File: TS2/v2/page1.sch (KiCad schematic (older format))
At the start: 25 parts, among them J1 74LS00, SW1 RESET

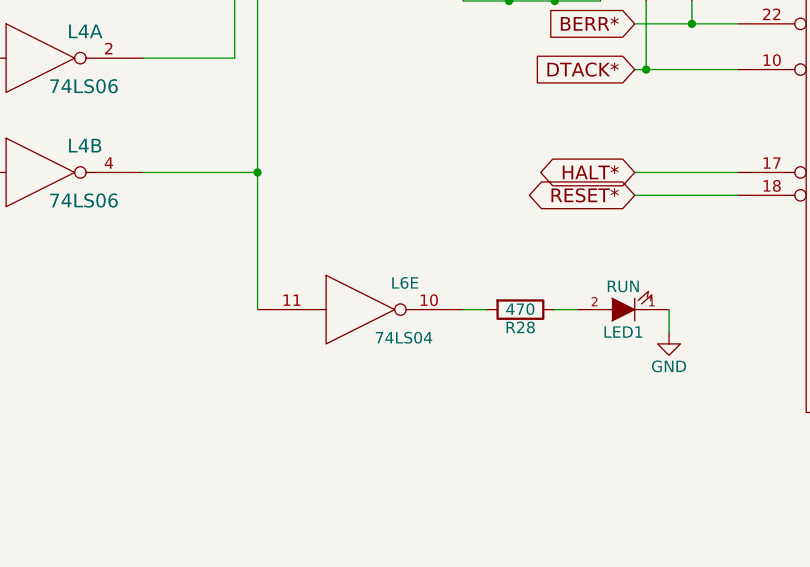
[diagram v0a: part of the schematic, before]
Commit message: Remove extra pages and renumber.
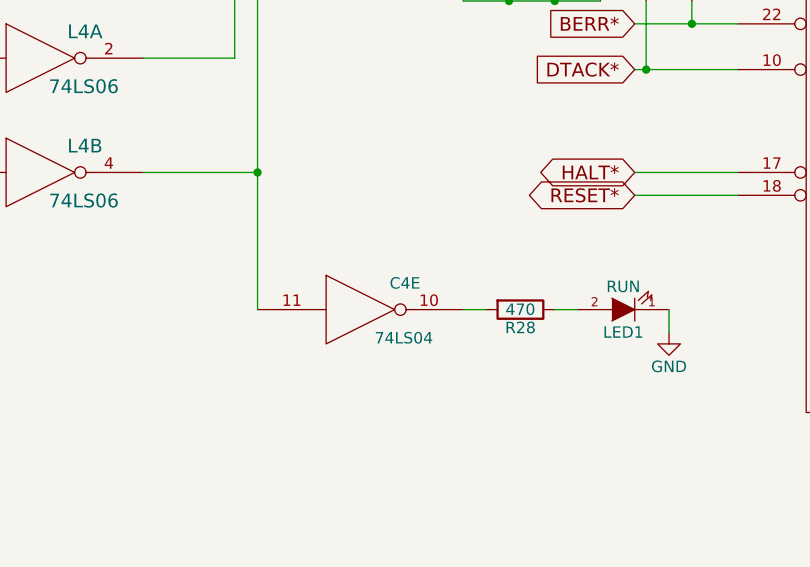
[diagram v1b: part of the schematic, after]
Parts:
- renumbered L6 to C4
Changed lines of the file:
@@
 NoConn ~ 7900 2900
 $Comp
-L 74LS04 L6
+L 74LS04 C4
 U 5 1 57CAED80
 P 6250 5500
-F 0 "L6" H 6445 5615 50  0000 C CNN
+F 0 "C4" H 6445 5615 50  0000 C CNN
 F 1 "74LS04" H 6440 5375 50  0000 C CNN
 F 2 "" H 6250 5500 50  0000 C CNN

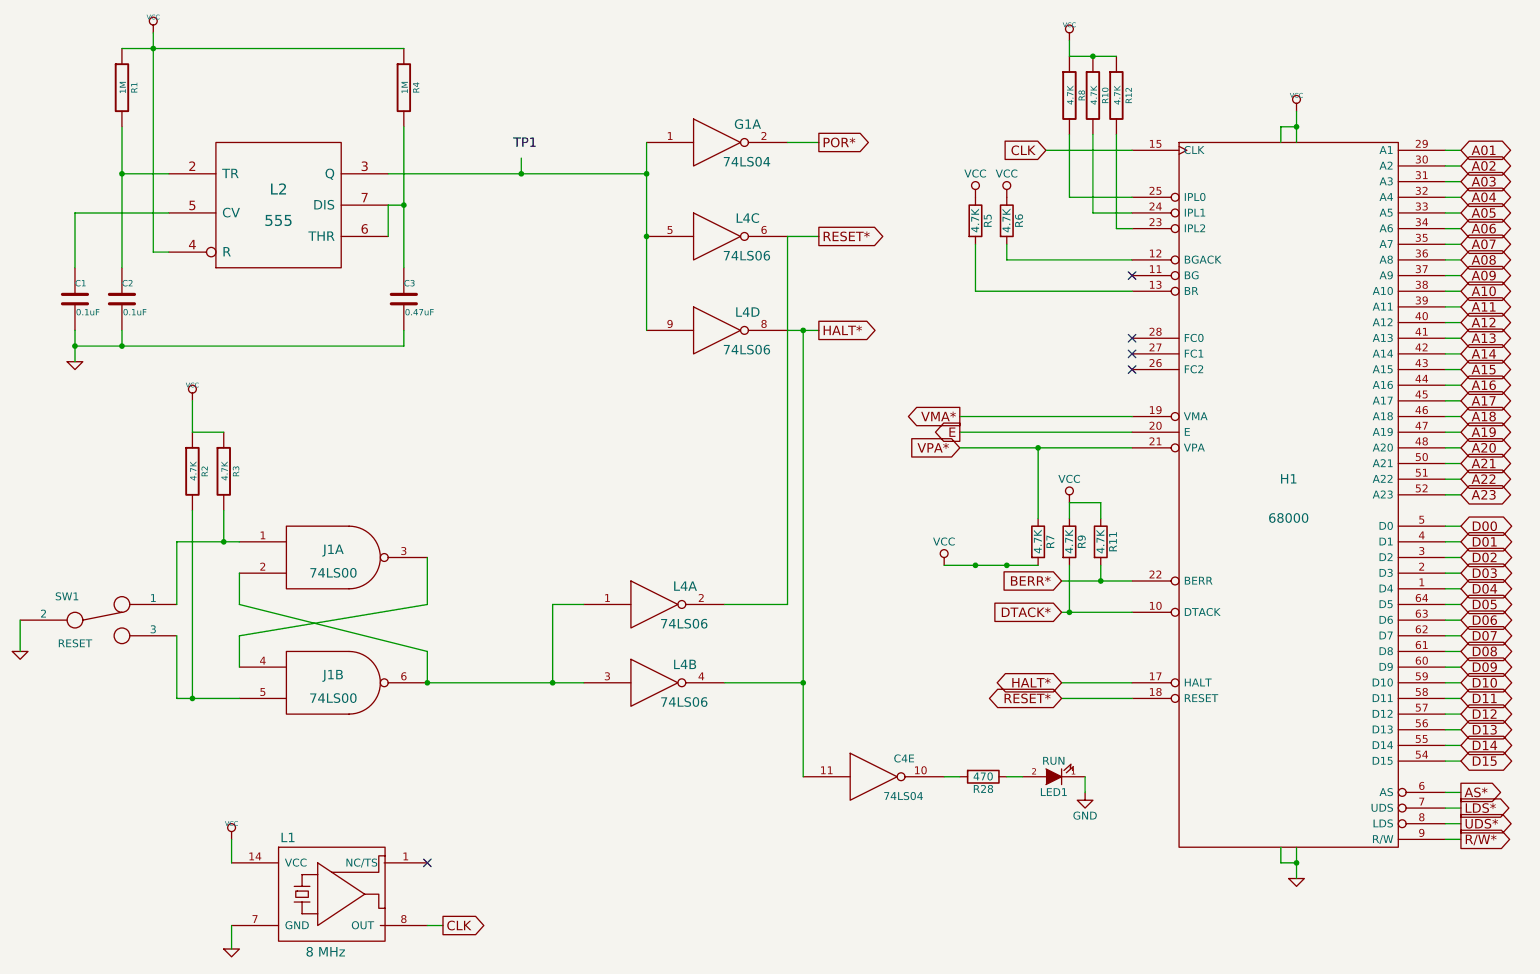
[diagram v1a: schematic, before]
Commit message: more fixup of deleted pages.
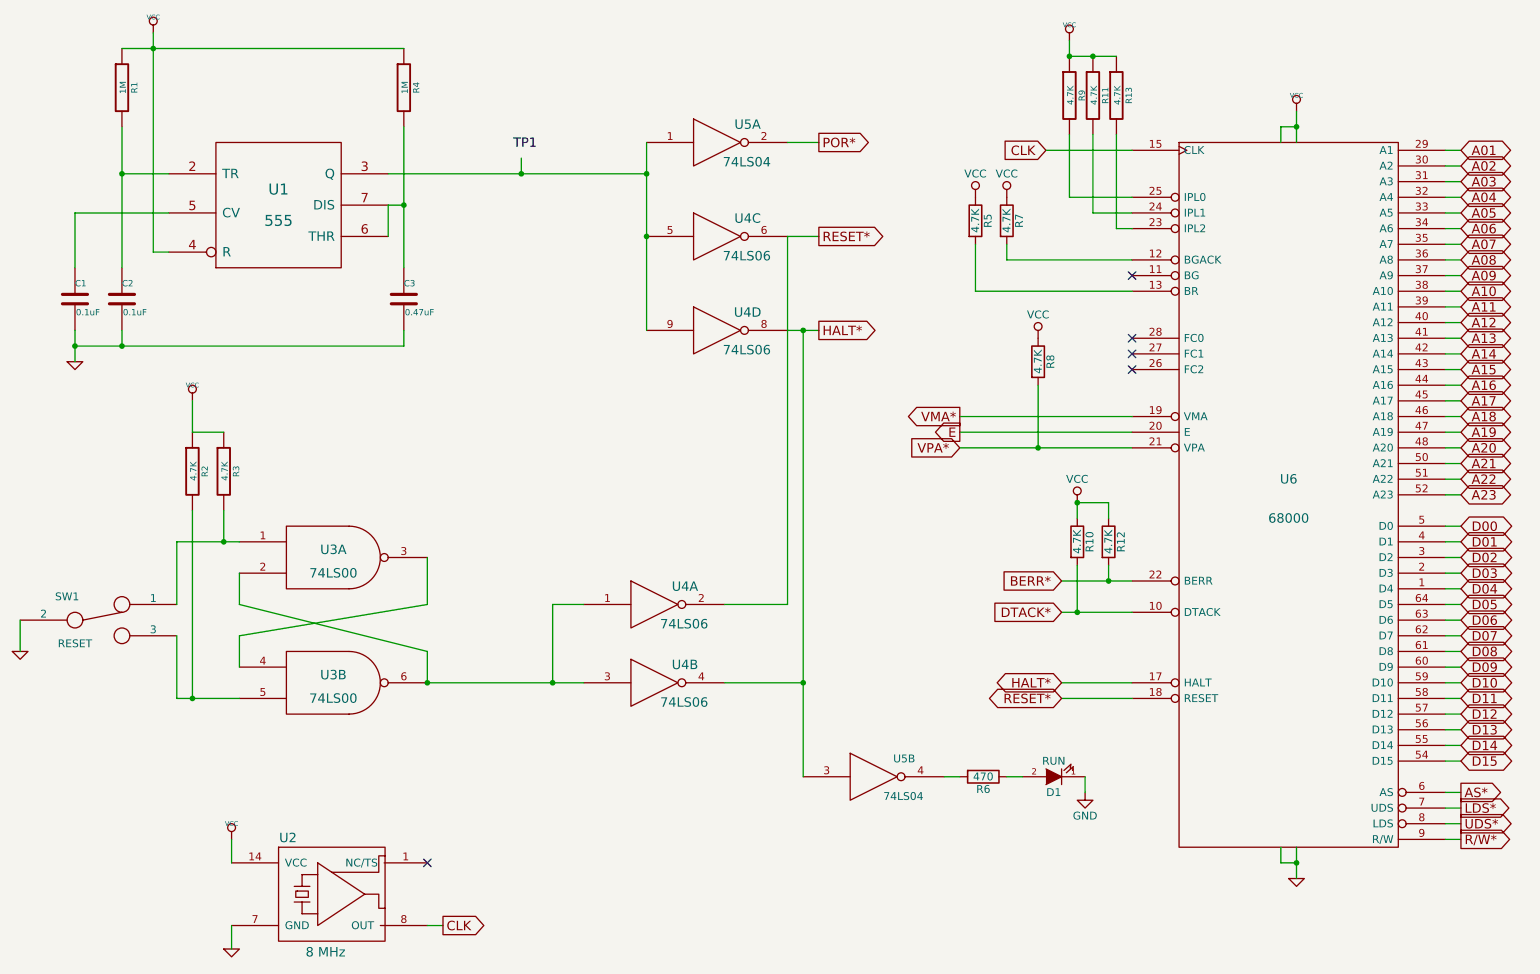
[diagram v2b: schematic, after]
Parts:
- renumbered LED1 to D1, R9 to R10, R10 to R11, R11 to R12, R12 to R13, R28 to R6, R6 to R7, R7 to R8, R8 to R9, L2 to U1, L1 to U2, J1 to U3, L4 to U4, G1 to U5, C4 to U5, H1 to U6
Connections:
- net HALT*: now also U5.3; no longer U5.11
- net VCC: now also R8.1; no longer R8.2
- net VPA*: now also R8.2; no longer R8.1
- net at R6.2: now also U5.4; no longer U5.10
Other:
- moved on the sheet: R10, R12, R8
